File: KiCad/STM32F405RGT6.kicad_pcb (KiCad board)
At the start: 4 copper layers, 101.6 x 101.6 mm, 10 parts, among them J201 Conn_02x32_Odd_Even, J202 Conn_02x20_Odd_Even, U1 STM32F405RGTx

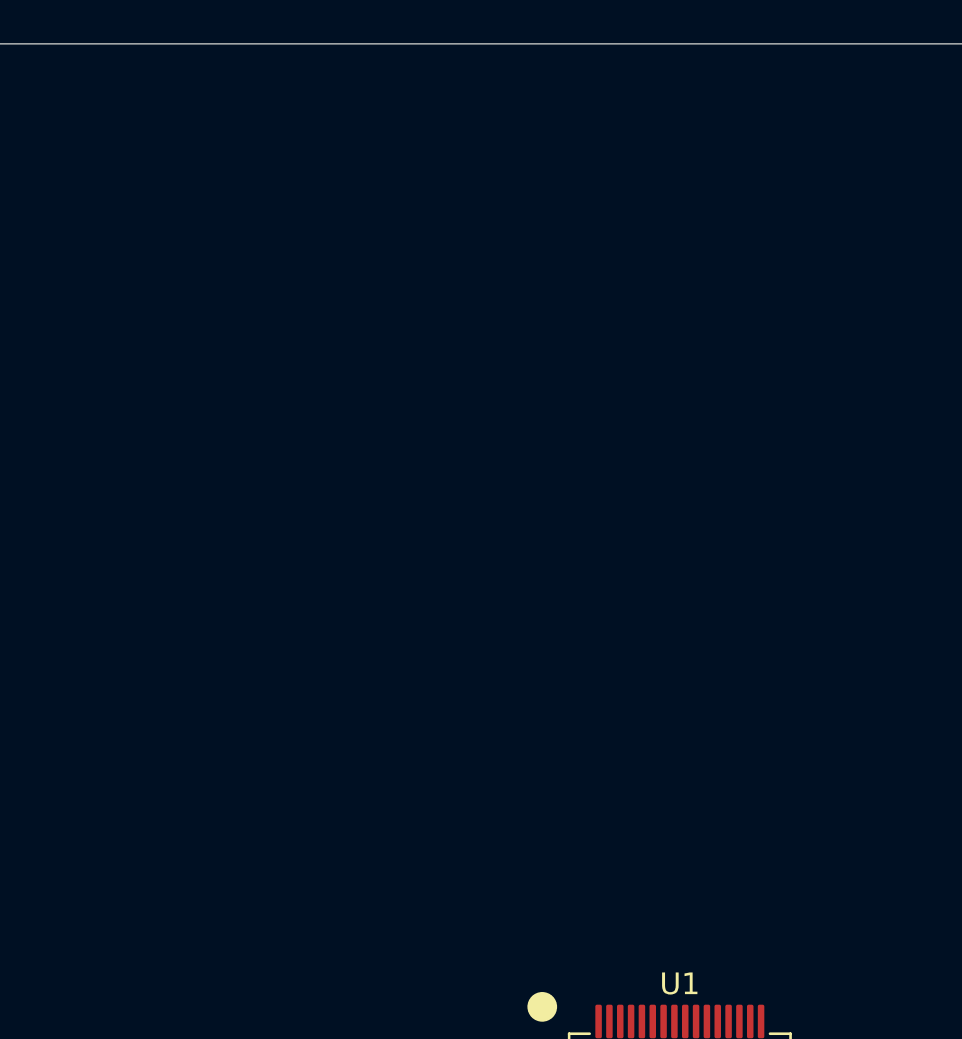
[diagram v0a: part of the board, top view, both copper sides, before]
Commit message: Added prototype components to schematic
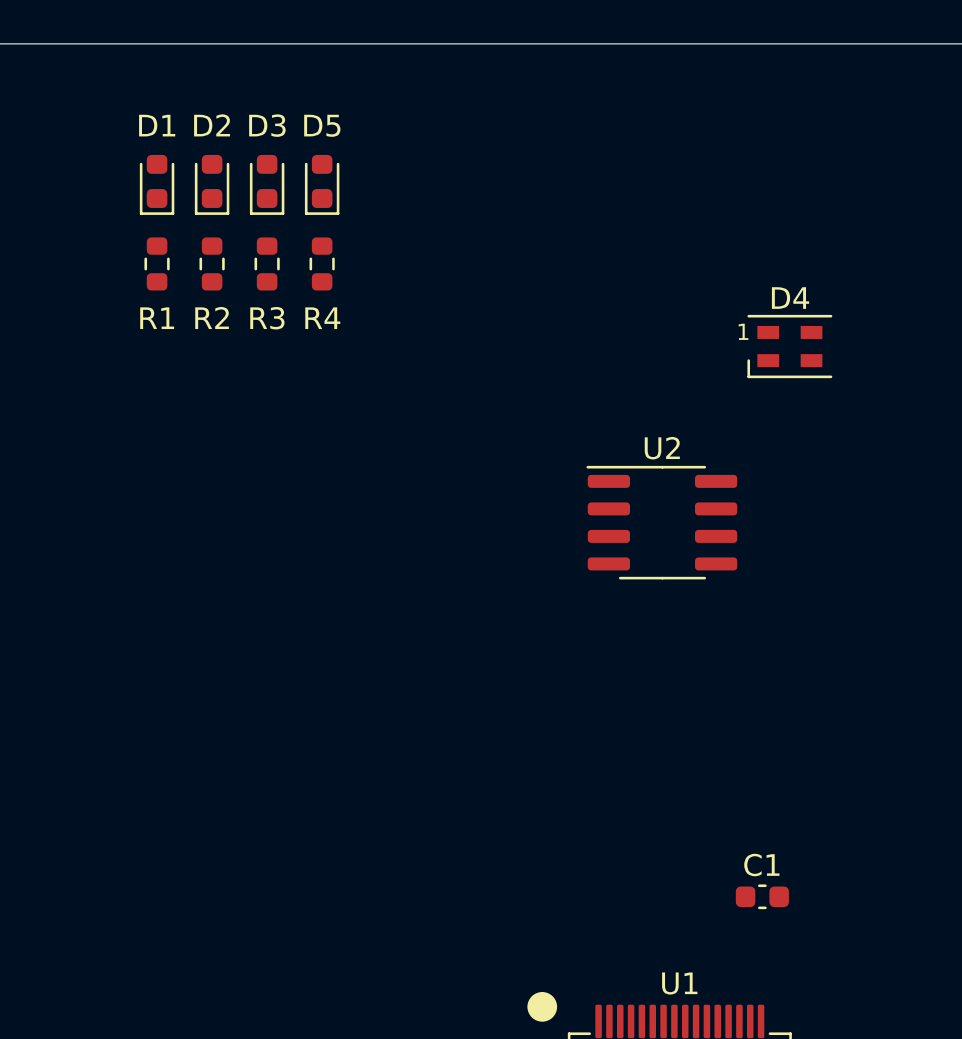
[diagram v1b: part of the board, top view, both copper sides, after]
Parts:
- added C1: 100nF, Capacitor_SMD:C_0603_1608Metric, F.Cu at (148.7, 73.3)
- added D1: LED_Small, LED_SMD:LED_0603_1608Metric, F.Cu at (120.8, 40.3)
- added D2: LED_Small, LED_SMD:LED_0603_1608Metric, F.Cu at (123.3, 40.3)
- added D3: LED_Small, LED_SMD:LED_0603_1608Metric, F.Cu at (125.9, 40.3)
- added D4: SK6805, LED_SMD:LED_SK6805_PLCC4_2.4x2.7mm_P1.3mm, F.Cu at (150.0, 47.9)
- added D5: LED_Small, LED_SMD:LED_0603_1608Metric, F.Cu at (128.4, 40.3)
- added R1: 1k, Resistor_SMD:R_0603_1608Metric, F.Cu at (120.8, 44.1)
- added R2: 1k, Resistor_SMD:R_0603_1608Metric, F.Cu at (123.3, 44.1)
- added R3: 1k, Resistor_SMD:R_0603_1608Metric, F.Cu at (125.9, 44.1)
- added R4: 1k, Resistor_SMD:R_0603_1608Metric, F.Cu at (128.4, 44.1)
- added U2: AT24CS64-SSHM, Package_SO:SOIC-8_3.9x4.9mm_P1.27mm, F.Cu at (144.1, 56.1)
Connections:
- U1 pad 12: unconnected-(U1-Pad12) -> GND
- U1 pad 18: unconnected-(U1-Pad18) -> GND
- U1 pad 63: unconnected-(U1-Pad63) -> GND

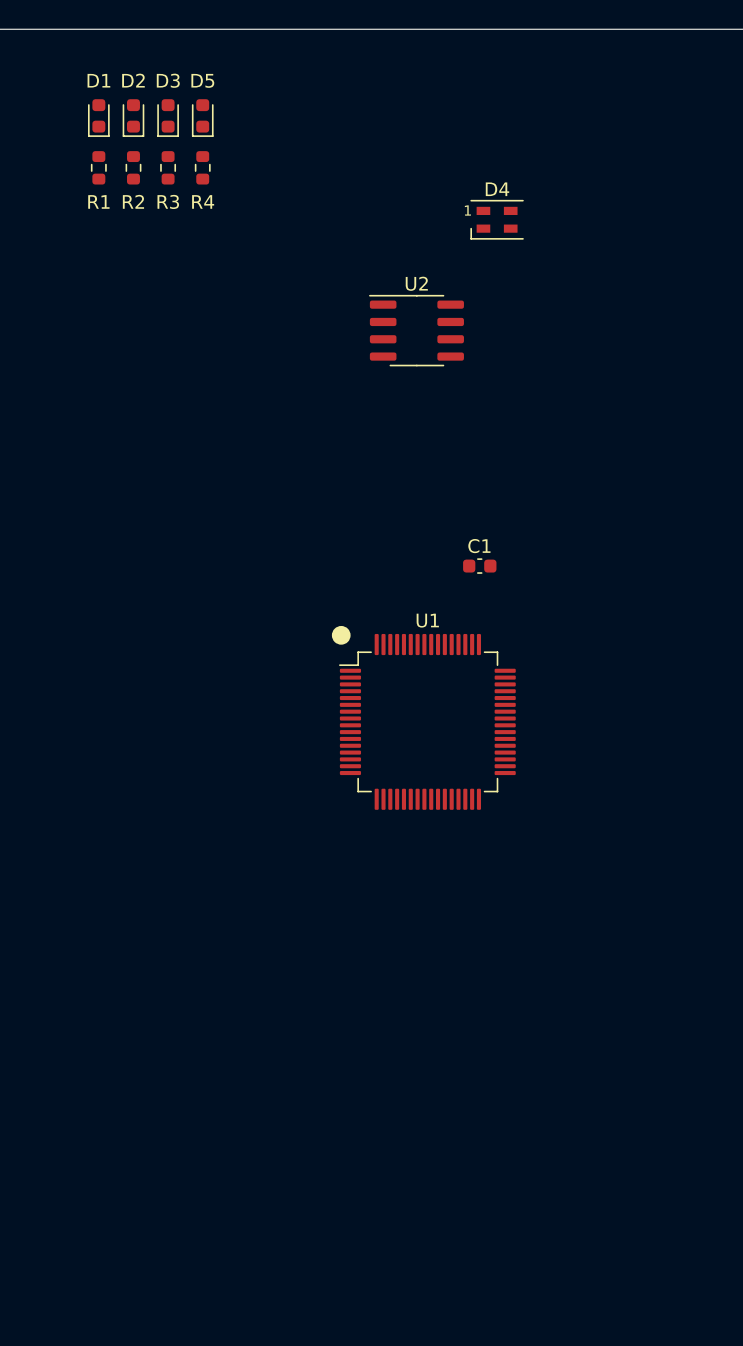
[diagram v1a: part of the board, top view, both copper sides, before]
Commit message: Added Components to the Schematic and PCB
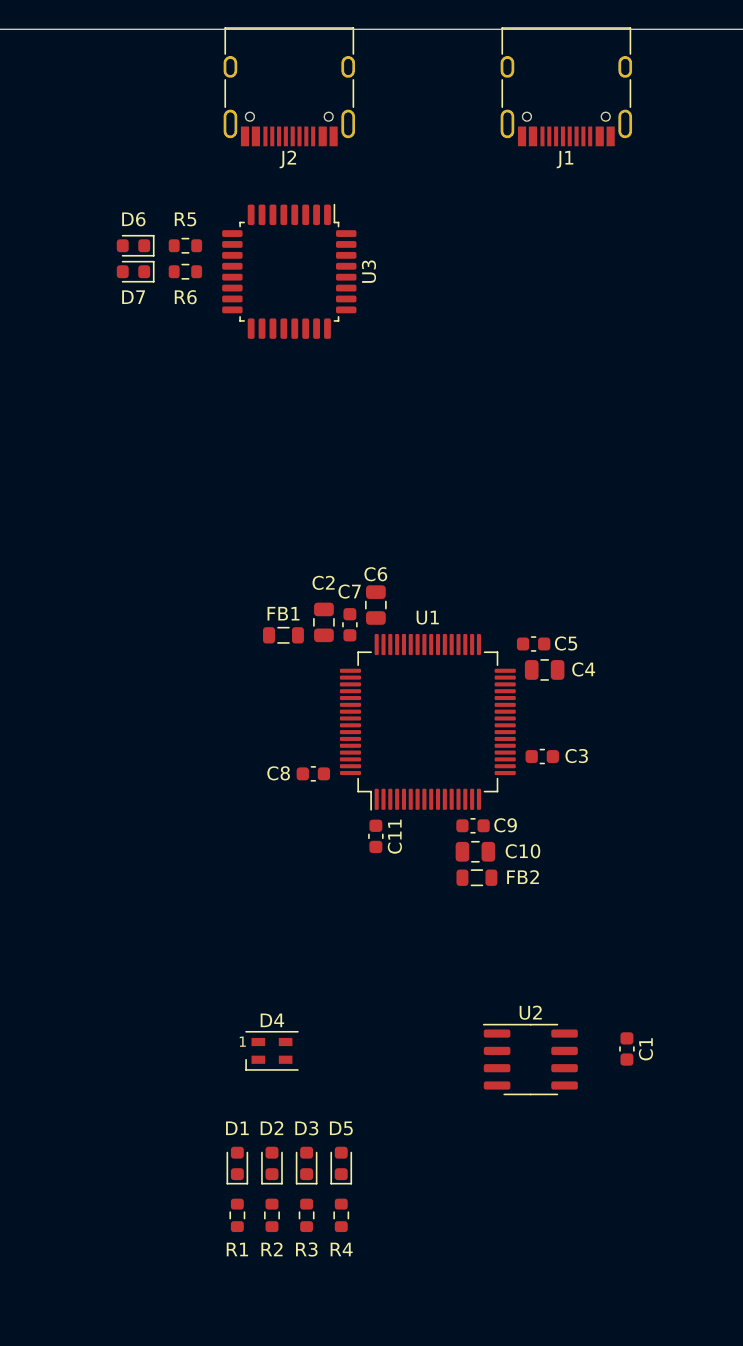
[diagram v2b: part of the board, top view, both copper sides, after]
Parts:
- added C10: 1uF, Capacitor_SMD:C_0805_2012Metric, F.Cu at (148.4, 94.3)
- added C11: 100nF, Capacitor_SMD:C_0603_1608Metric, F.Cu at (141.1, 93.2)
- added C2: 10uF, Capacitor_SMD:C_0805_2012Metric, F.Cu at (137.3, 77.5)
- added C3: 100nF, Capacitor_SMD:C_0603_1608Metric, F.Cu at (153.3, 87.3)
- added C4: 2.2uF, Capacitor_SMD:C_0805_2012Metric, F.Cu at (153.5, 81.0)
- added C5: 100nF, Capacitor_SMD:C_0603_1608Metric, F.Cu at (152.7, 79.0)
- added C6: 2.2uF, Capacitor_SMD:C_0805_2012Metric, F.Cu at (141.1, 76.2)
- added C7: 100nF, Capacitor_SMD:C_0603_1608Metric, F.Cu at (139.2, 77.6)
- added C8: 100nF, Capacitor_SMD:C_0603_1608Metric, F.Cu at (136.5, 88.6)
- added C9: 100nF, Capacitor_SMD:C_0603_1608Metric, F.Cu at (148.2, 92.4)
- added D6: LED_Small, LED_SMD:LED_0603_1608Metric, F.Cu at (123.3, 49.8)
- added D7: LED_Small, LED_SMD:LED_0603_1608Metric, F.Cu at (123.3, 51.7)
- added FB1: FerriteBead_Small, Inductor_SMD:L_0805_2012Metric, F.Cu at (134.3, 78.4)
- added FB2: FerriteBead_Small, Inductor_SMD:L_0805_2012Metric, F.Cu at (148.5, 96.2)
- added J1: USB_C_Receptacle_USB2.0, Connector_USB:USB_C_Receptacle_HRO_TYPE-C-31-M-12, F.Cu at (155.1, 37.8)
- added J2: USB_C_Receptacle_USB2.0, Connector_USB:USB_C_Receptacle_HRO_TYPE-C-31-M-12, F.Cu at (134.8, 37.8)
- added R5: 1k, Resistor_SMD:R_0603_1608Metric, F.Cu at (127.1, 49.8)
- added R6: 1k, Resistor_SMD:R_0603_1608Metric, F.Cu at (127.1, 51.7)
- added U3: FT232BM, Package_QFP:LQFP-32_7x7mm_P0.8mm, F.Cu at (134.8, 51.7)
- moved R1 77.5 mm to (130.9, 121.0)
- moved R2 77.5 mm to (133.5, 121.0)
- moved R3 77.5 mm to (136.0, 121.0)
- moved R4 77.5 mm to (138.6, 121.0)
- moved D1 77.5 mm to (130.9, 117.1)
- moved D2 77.5 mm to (133.5, 117.1)
- moved D3 77.5 mm to (136.0, 117.1)
- moved D5 77.5 mm to (138.6, 117.1)
- moved D4 63.2 mm to (133.5, 108.9)
- moved U2 54.1 mm to (152.5, 109.5)
- moved C1 37.0 mm to (159.5, 108.8), turned to -90 degrees
- turned U1 to 90 degrees
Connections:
- C1 pad 1: unconnected-(C1-Pad1) -> FTDI_RST
- C1 pad 2: unconnected-(C1-Pad2) -> GND
- J201 pad 11: +3V3 -> FTDI_RST
- J201 pad 63: +3V3 -> FTDI_RST
- U1 pad 1: unconnected-(U1-Pad1) -> /VDD_Decoupling
- U1 pad 13: unconnected-(U1-Pad13) -> /VDDA_Decoupling
- U1 pad 19: unconnected-(U1-Pad19) -> /VDD_Decoupling
- U1 pad 31: unconnected-(U1-Pad31) -> Net-(C4-Pad1)
- U1 pad 32: unconnected-(U1-Pad32) -> /VDD_Decoupling
- U1 pad 35: unconnected-(U1-Pad35) -> /STM32_USBD-
- U1 pad 36: unconnected-(U1-Pad36) -> /STM32_USBD+
- U1 pad 42: unconnected-(U1-Pad42) -> FTDI_RX
- U1 pad 43: unconnected-(U1-Pad43) -> FTDI_TX
- U1 pad 47: unconnected-(U1-Pad47) -> Net-(C6-Pad1)
- U1 pad 48: unconnected-(U1-Pad48) -> /VDD_Decoupling
- U1 pad 64: unconnected-(U1-Pad64) -> /VDD_Decoupling
- U1 pad 7: unconnected-(U1-Pad7) -> FTDI_RST

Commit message: Updated Schematic and PCB
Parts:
- added C12: 14pF, Capacitor_SMD:C_0603_1608Metric, F.Cu at (148.1, 100.6)
- added C13: 14pF, Capacitor_SMD:C_0603_1608Metric, F.Cu at (154.4, 100.6)
- added JP1: BOOT0, Connector_PinHeader_2.54mm:PinHeader_1x02_P2.54mm_Vertical, F.Cu at (212.9, 93.7)
- added R7: 10k, Resistor_SMD:R_0603_1608Metric, F.Cu at (216.0, 94.5)
- added R8: 470R, Resistor_SMD:R_0603_1608Metric, F.Cu at (152.5, 96.8)
- added R9: 10k, Resistor_SMD:R_0603_1608Metric, F.Cu at (228.9, 84.8)
- added Y1: 25MHz, Crystal:Crystal_SMD_3225-4Pin_3.2x2.5mm, F.Cu at (151.3, 100.6)
- D4: footprint LED_SMD:LED_SK6805_PLCC4_2.4x2.7mm_P1.3mm -> LED_SMD:LED_SK6812_EC15_1.5x1.5mm
- FB1, FB2: value FerriteBead_Small -> 100R @100MHz
- moved D4 102.7 mm to (235.1, 93.7)
- moved C8 82.0 mm to (218.4, 92.4)
- moved C11 76.5 mm to (217.3, 86.0)
- moved C2 75.6 mm to (212.9, 79.4)
- moved C4 75.6 mm to (229.1, 82.9)
- moved C5 75.6 mm to (228.2, 81.0)
- moved C6 75.6 mm to (216.7, 78.1)
- moved C7 75.6 mm to (214.8, 79.5)
- moved FB1 75.6 mm to (209.9, 80.3)
- moved C10 75.0 mm to (223.3, 97.5)
- moved FB2 75.0 mm to (223.5, 99.4)
- moved C9 75.0 mm to (223.2, 95.6)
- moved C1 70.2 mm to (227.5, 91.1)
- moved C3 68.7 mm to (222.0, 86.7)
- moved J1 30.5 mm to (124.6, 37.8)
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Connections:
- net Net-(C4-Pad1) renamed /VCAP_1
- net Net-(C6-Pad1) renamed /VCAP_2
- U1 pad 28: unconnected-(U1-Pad28) -> Net-(U1-Pad28)
- U1 pad 5: unconnected-(U1-Pad5) -> /HSE_IN
- U1 pad 6: unconnected-(U1-Pad6) -> /HSE_OUT
- U1 pad 60: unconnected-(U1-Pad60) -> /BOOT0

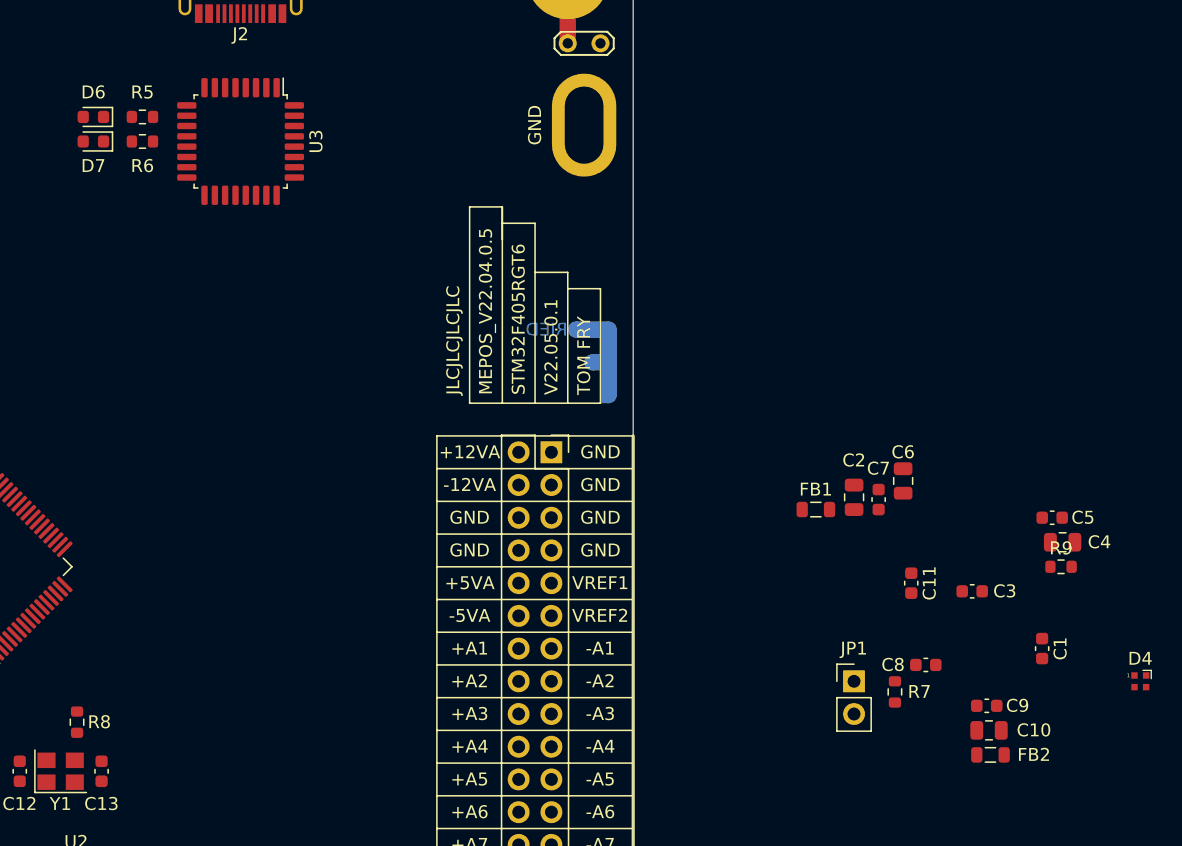
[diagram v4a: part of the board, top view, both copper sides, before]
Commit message: Added components to schematic
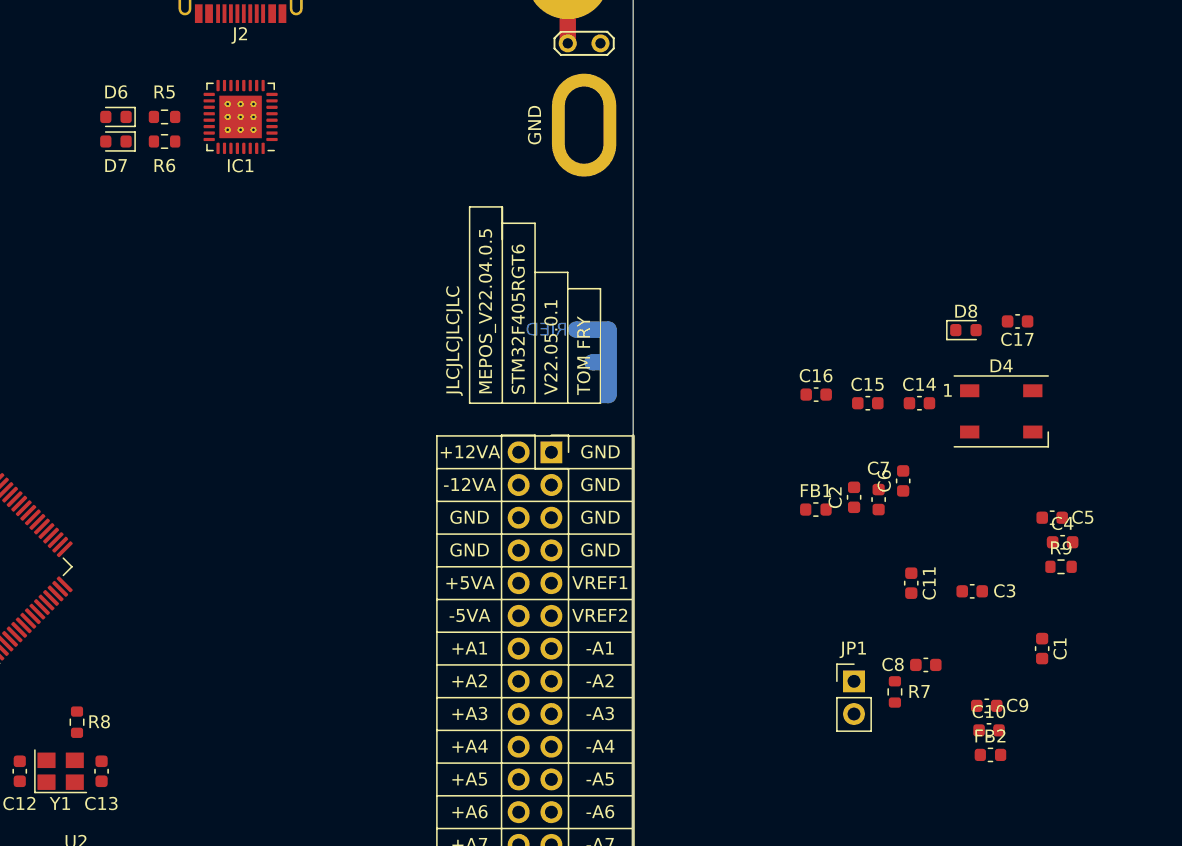
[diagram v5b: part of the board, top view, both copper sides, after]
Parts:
- removed U3: FT232BM, Package_QFP:LQFP-32_7x7mm_P0.8mm
- added C14: 100nF, Capacitor_SMD:C_0603_1608Metric, F.Cu at (217.9, 72.1)
- added C15: 100nF, Capacitor_SMD:C_0603_1608Metric, F.Cu at (213.9, 72.1)
- added C16: 10uF, Capacitor_SMD:C_0603_1608Metric, F.Cu at (209.9, 71.4)
- added C17: 100nF, Capacitor_SMD:C_0603_1608Metric, F.Cu at (225.6, 65.7)
- added D8: D_Small, Diode_SMD:D_0603_1608Metric, F.Cu at (221.6, 66.4)
- added IC1: FT232RQ-REEL, Package_DFN_QFN:QFN-32-1EP_5x5mm_P0.5mm_EP3.3x3.3mm_ThermalVias, F.Cu at (165.2, 49.8)
- C10, C2, C4, C6: footprint Capacitor_SMD:C_0805_2012Metric -> Capacitor_SMD:C_0603_1608Metric
- D4: value SK6805 -> WS2812B; footprint LED_SMD:LED_SK6812_EC15_1.5x1.5mm -> LED_SMD:LED_WS2812B_PLCC4_5.0x5.0mm_P3.2mm
- D6, D7: value LED_Small -> Red LED
- FB1, FB2: value 100R @100MHz -> 220R @100MHz; footprint Inductor_SMD:L_0805_2012Metric -> Inductor_SMD:L_0603_1608Metric
- moved D4 23.6 mm to (224.3, 72.7)
- moved D6 1.75 mm to (155.6, 49.8)
- moved D7 1.75 mm to (155.6, 51.7)
- moved R5 1.72 mm to (159.3, 49.8)
- moved R6 1.72 mm to (159.3, 51.7)
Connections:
- net /FTDI_USBD+ renamed FTDI_USBD+
- net /FTDI_USBD- renamed FTDI_USBD-
- D4 pad 1: unconnected-(D4-Pad1) -> /LED_Decoupling
- D4 pad 3: unconnected-(D4-Pad3) -> GND
- D4 pad 4: unconnected-(D4-Pad4) -> LED_DIN
